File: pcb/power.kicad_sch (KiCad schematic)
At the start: 33 parts, among them U5 REG_LDO_3V3_250mA_TI_LP5907MF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, U7 REG_SW_BOOST_TI_TLV61046ADBV

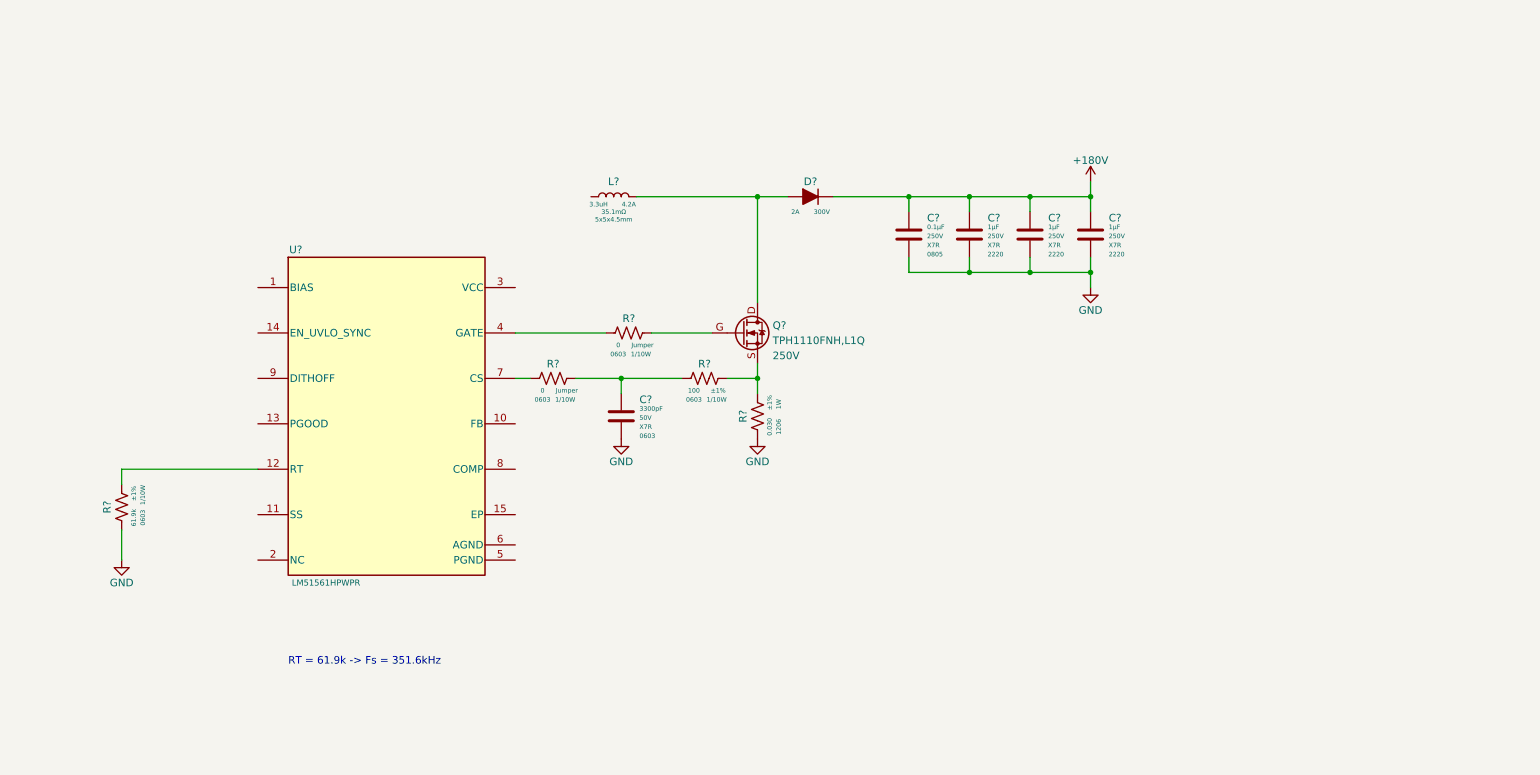
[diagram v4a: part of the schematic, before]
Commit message: Added soft start cap
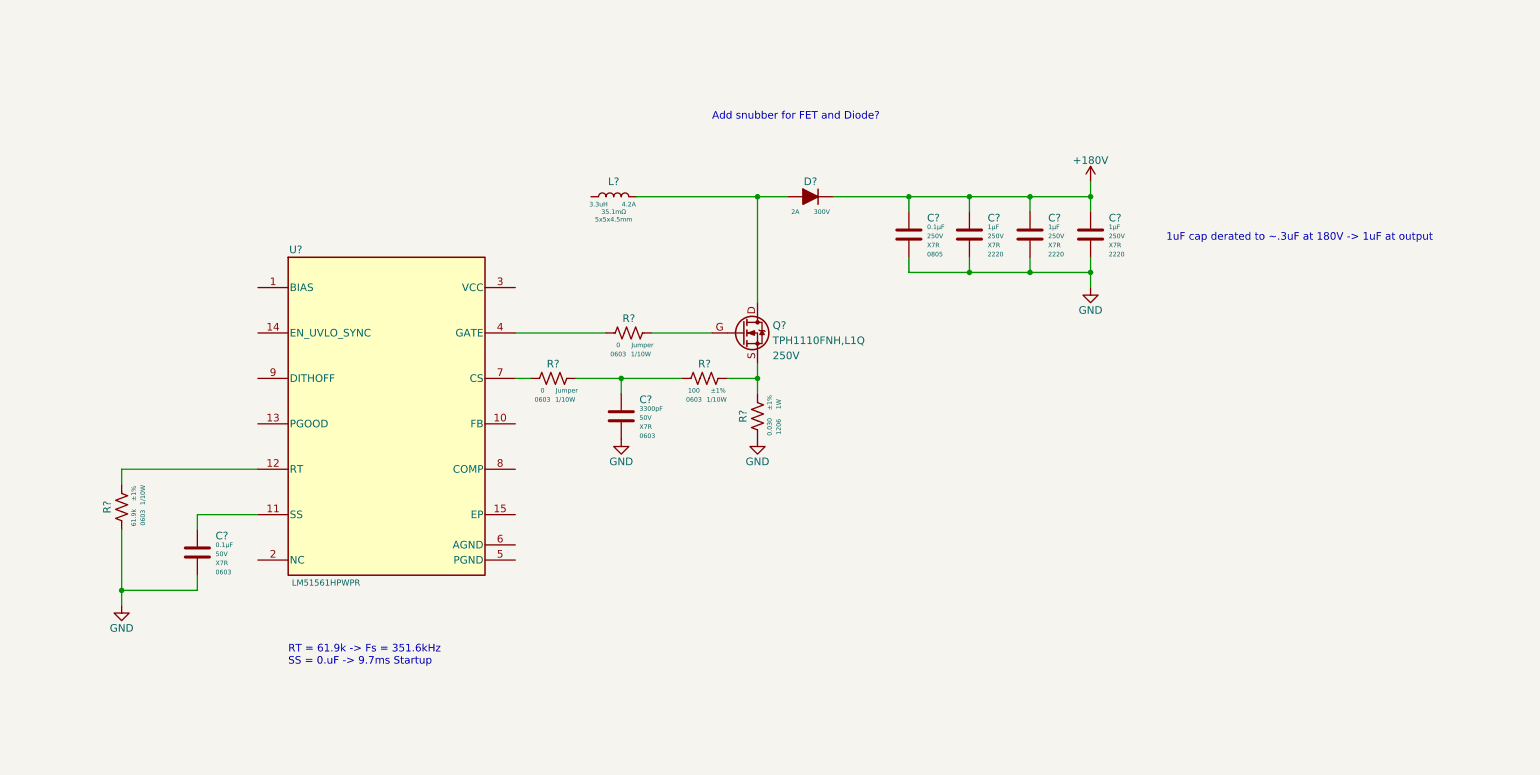
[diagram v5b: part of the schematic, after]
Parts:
- added C?: CAP_CER_0u1_50V_X7R_0603, Capacitor_SMD:C_0603_1608Metric, symbol arjun_symbols:CAP_CER_0u1_50V_X7R_0603
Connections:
- net GND: now also C?.2
- net at U?.11 (SS): now also C?.1
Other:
- note added: "1uF cap derated to ~.3uF at 180V -> 1uF at output"
- note added: "Add snubber for FET and Diode?"
- note added: "RT = 61.9k -> Fs = 351.6kHz SS = 0.uF -> 9.7ms Startup"
- note removed: "RT = 61.9k -> Fs = 351.6kHz"
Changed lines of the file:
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@@
   (junction (at 111.76 215.9) (diameter 0) (color 0 0 0 0)
   )
+  (junction (at 149.86 124.46) (diameter 0) (color 0 0 0 0)
+  )
   (junction (at 139.7 203.2) (diameter 0) (color 0 0 0 0)
   )
@@
     (stroke (width 0) (type default) (color 0 0 0 0))
   )
+  (wire (pts (xy 162.56 124.46) (xy 149.86 124.46))
+    (stroke (width 0) (type default) (color 0 0 0 0))
+  )
   (wire (pts (xy 104.14 73.66) (xy 106.68 73.66))
     (stroke (width 0) (type default) (color 0 0 0 0))
@@
     (stroke (width 0) (type default) (color 0 0 0 0))
   )
+  (wire (pts (xy 162.56 111.76) (xy 172.72 111.76))
+    (stroke (width 0) (type default) (color 0 0 0 0))
+  )
   (wire (pts (xy 88.9 185.42) (xy 99.06 185.42))
     (stroke (width 0) (type default) (color 0 0 0 0))
@@
     (stroke (width 0) (type default) (color 0 0 0 0))
   )
+  (wire (pts (xy 162.56 114.3) (xy 162.56 111.76))
+    (stroke (width 0) (type default) (color 0 0 0 0))
+  )
   (wire (pts (xy 246.38 213.36) (xy 246.38 215.9))
     (stroke (width 0) (type default) (color 0 0 0 0))
@@
     (stroke (width 0) (type default) (color 0 0 0 0))
   )
-  (wire (pts (xy 149.86 114.3) (xy 149.86 119.38))
+  (wire (pts (xy 149.86 114.3) (xy 149.86 124.46))
     (stroke (width 0) (type default) (color 0 0 0 0))
   )
@@
     (stroke (width 0) (type default) (color 0 0 0 0))
   )
+  (wire (pts (xy 149.86 124.46) (xy 149.86 127))
+    (stroke (width 0) (type default) (color 0 0 0 0))
+  )
   (wire (pts (xy 129.54 203.2) (xy 129.54 205.74))
     (stroke (width 0) (type default) (color 0 0 0 0))
@@
   )
   (wire (pts (xy 287.02 200.66) (xy 294.64 200.66))
+    (stroke (width 0) (type default) (color 0 0 0 0))
+  )
+  (wire (pts (xy 162.56 121.92) (xy 162.56 124.46))
     (stroke (width 0) (type default) (color 0 0 0 0))
   )
@@
     (effects (font (size 1.27 1.27)) (justify left bottom))
   )
+  (text "Add snubber for FET and Diode?\n" (at 248.92 45.72 0)
+    (effects (font (size 1.27 1.27)) (justify left bottom))
+  )
   (text "!! Add LEDs\n!! Add Test points\n" (at 21.59 25.4 0)
     (effects (font (size 1.27 1.27)) (justify left bottom))
@@
     (effects (font (size 1.27 1.27)) (justify left bottom))
   )
-  (text "RT = 61.9k -> Fs = 351.6kHz\n" (at 177.8 137.16 0)
+  (text "1uF cap derated to ~.3uF at 180V -> 1uF at output\n"
+    (at 325.12 66.04 0)
+    (effects (font (size 1.27 1.27)) (justify left bottom))
+  )
+  (text "RT = 61.9k -> Fs = 351.6kHz\nSS = 0.uF -> 9.7ms Startup"
+    (at 177.8 137.16 0)
     (effects (font (size 1.27 1.27)) (justify left bottom))
   )
@@
     (pin "1")
   )
-  (symbol (lib_id "power:GND") (at 149.86 119.38 0) (unit 1)
-    (in_bom yes) (on_board yes)
-    (property "Reference" "#PWR?" (id 0) (at 149.86 125.73 0)
-      (effects (font (size 1.27 1.27)) hide)
-    )
-    (property "Value" "GND" (id 1) (at 149.86 123.19 0))
-    (property "Footprint" "" (id 2) (at 149.86 119.38 0)
-      (effects (font (size 1.27 1.27)) hide)
-    )
-    (property "Datasheet" "" (id 3) (at 149.86 119.38 0)
+  (symbol (lib_id "power:GND") (at 149.86 127 0) (unit 1)
+    (in_bom yes) (on_board yes)
+    (property "Reference" "#PWR?" (id 0) (at 149.86 133.35 0)
+      (effects (font (size 1.27 1.27)) hide)
+    )
+    (property "Value" "GND" (id 1) (at 149.86 130.81 0))
+    (property "Footprint" "" (id 2) (at 149.86 127 0)
+      (effects (font (size 1.27 1.27)) hide)
+    )
+    (property "Datasheet" "" (id 3) (at 149.86 127 0)
       (effects (font (size 1.27 1.27)) hide)
     )
@@
     (pin "6")
   )
+  (symbol (lib_id "arjun_symbols:CAP_CER_0u1_50V_X7R_0603") (at 162.56 114.3 0) (unit 1)
+    (in_bom yes) (on_board yes)
+    (property "Reference" "C?" (id 0) (at 165.608 115.316 0)
+      (effects (font (size 1.27 1.27)) (justify left))
+    )
+    (property "Value" "CAP_CER_0u1_50V_X7R_0603" (id 1) (at 170.18 109.855 0)
+      (effects (font (size 1.27 1.27)) (justify left) hide)
+    )
+    (property "Footprint" "Capacitor_SMD:C_0603_1608Metric" (id 2) (at 170.18 111.76 0)
+      (effects (font (size 1.27 1.27)) (justify left) hide)
+    )
+    (property "Datasheet" "https://search.murata.co.jp/Ceramy/image/img/A01X/G101/ENG/GRM21BR61H475KE51-01.pdf" (id 3) (at 170.18 121.92 0)
+      (effects (font (size 1.27 1.27)) (justify left) hide)
+    )
+    (property "Manufacturer" "Samsung Electro-Mechanics" (id 4) (at 170.18 116.84 0)
+      (effects (font (size 1.27 1.27)) (justify left) hide)
+    )
+    (property "ManufacturerPN" "CL10B104KB8NNNC" (id 5) (at 170.18 119.38 0)
+      (effects (font (size 1.27 1.27)) (justify left) hide)
+    )
+    (property "Vendor" "Digi-Key" (id 6) (at 170.18 124.46 0)
+      (effects (font (size 1.27 1.27)) (justify left) hide)
+    )
+    (property "VendorPN" "1276-1000-1-ND" (id 7) (at 170.18 127 0)
+      (effects (font (size 1.27 1.27)) (justify left) hide)
+    )
+    (property "Capacitance" "0.1µF" (id 8) (at 165.608 116.84 0)
+      (effects (font (size 0.762 0.762)) (justify left))
+    )
+    (property "Voltage" "50V" (id 9) (at 165.608 118.364 0)
+      (effects (font (size 0.762 0.762)) (justify left))
+    )
+    (property "Package" "0603" (id 10) (at 165.608 121.412 0)
+      (effects (font (size 0.762 0.762)) (justify left))
+    )
+    (property "Temp Co" "X7R" (id 11) (at 165.608 119.888 0)
+      (effects (font (size 0.762 0.762)) (justify left))
+    )
+    (pin "1")
+    (pin "2")
+  )
   (symbol (lib_id ".arjun:FER_120R_2A_0603") (at 231.14 200.66 0) (unit 1)

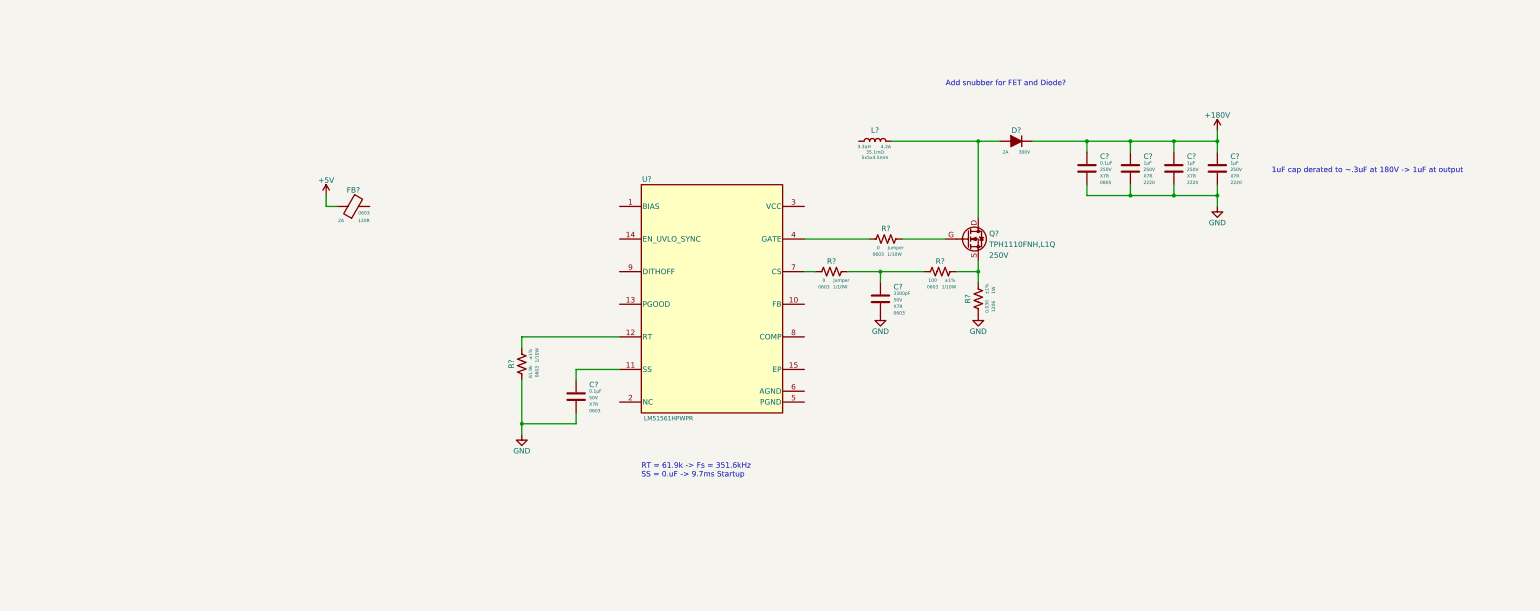
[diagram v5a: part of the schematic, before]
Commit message: Added most of the passives for the 180V supply
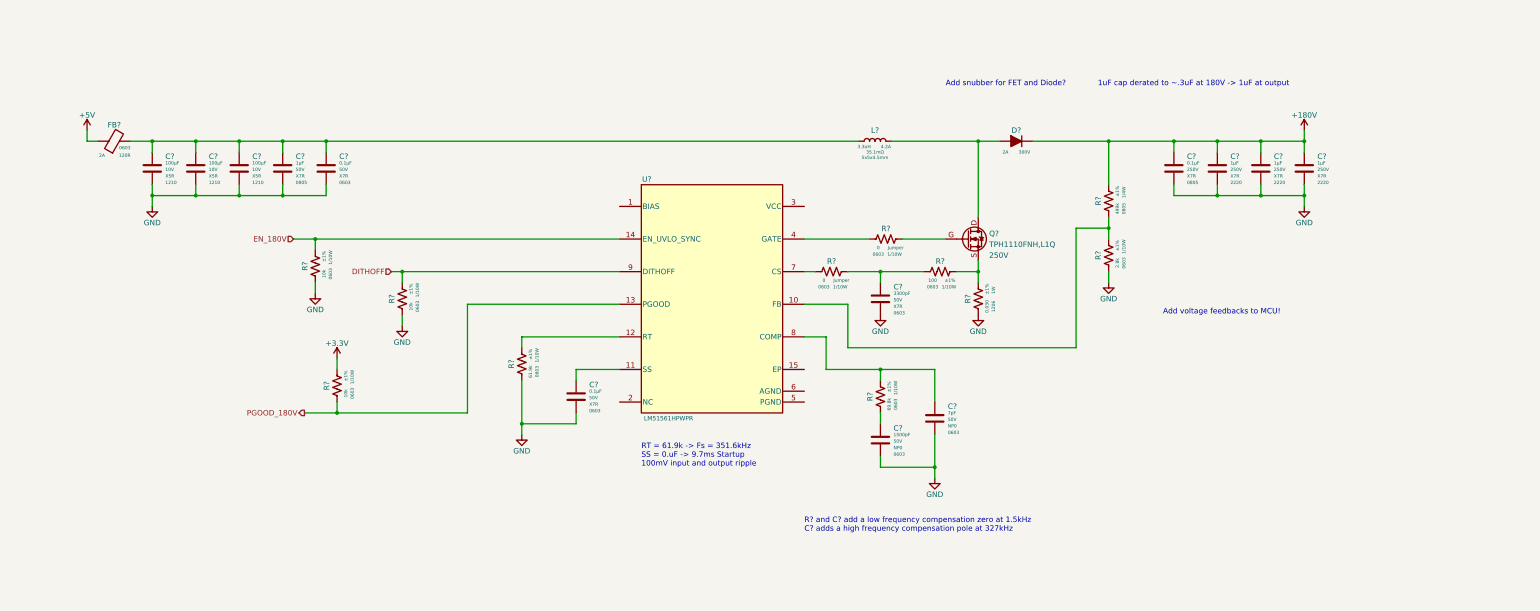
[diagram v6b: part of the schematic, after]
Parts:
- added C? (x3): CAP_CER_100u_10V_X5R_1210, Capacitor_SMD:C_1210_3225Metric, symbol .arjun:CAP_CER_100u_10V_X5R_1210
- added C?: CAP_CER_7p_50V_NP0_0603, Capacitor_SMD:C_0603_1608Metric, symbol .arjun:CAP_CER_7p_50V_NP0_0603
- added C?: CAP_CER_1u_50V_X7R_0805, Capacitor_SMD:C_0805_2012Metric, symbol .arjun:CAP_CER_1u_50V_X7R_0805
- added C?: CAP_CER_1500p_50V_NP0_0603, Capacitor_SMD:C_0603_1608Metric, symbol .arjun:CAP_CER_1500p_50V_NP0_0603
- added C?: CAP_CER_0u1_50V_X7R_0603, Capacitor_SMD:C_0603_1608Metric, symbol arjun_symbols:CAP_CER_0u1_50V_X7R_0603
- added R?: RES_2K8_1P_1/10W_0603, Resistor_SMD:R_0603_1608Metric, symbol .arjun:RES_2K8_1P_1/10W_0603
- added R? (x3): RES_10K_1P_1/10W_0603, Resistor_SMD:R_0603_1608Metric, symbol .arjun:RES_10K_1P_1/10W_0603
- added R?: RES_499K_1P_1/4W_0805, Resistor_SMD:R_0805_2012Metric, symbol .arjun:RES_499K_1P_1/4W_0805
- added R?: RES_69K8_1P_1/10W_0603, Resistor_SMD:R_0603_1608Metric, symbol .arjun:RES_69K8_1P_1/10W_0603
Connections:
- net +3.3V: now also R?.1
- net 180V: now also R?.1
- net GND: now also C?.2, C?.2, C?.2, C?.2, C?.2, C?.2, C?.2, R?.2, R?.2, R?.2
- net at U?.10 (FB): now also R?.1, R?.2
- net PGOOD_180V: now reaches U?.13 (PGOOD)
- net PGOOD_180V: now also R?.2
- net EN_180V: now reaches U?.14 (EN_UVLO_SYNC)
- net EN_180V: now also R?.1
- net at U?.8 (COMP): now also C?.1, R?.1
- net DITHOFF: now reaches U?.9 (DITHOFF)
- net DITHOFF: now also R?.1
- net at FB?.2: now also L?.1, C?.1, C?.1, C?.1, C?.1, C?.1
- new net: C?.1, R?.2
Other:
- note added: "Add voltage feedbacks to MCU!"
- note added: "R? and C? add a low frequency compensation zero at 1.5kHz C? adds a high frequency compensation pole at 327kHz"
- note added: "RT = 61.9k -> Fs = 351.6kHz SS = 0.uF -> 9.7ms Startup 100mV input and output ripple"
- note removed: "RT = 61.9k -> Fs = 351.6kHz SS = 0.uF -> 9.7ms Startup"
- moved on the sheet: C?, FB?

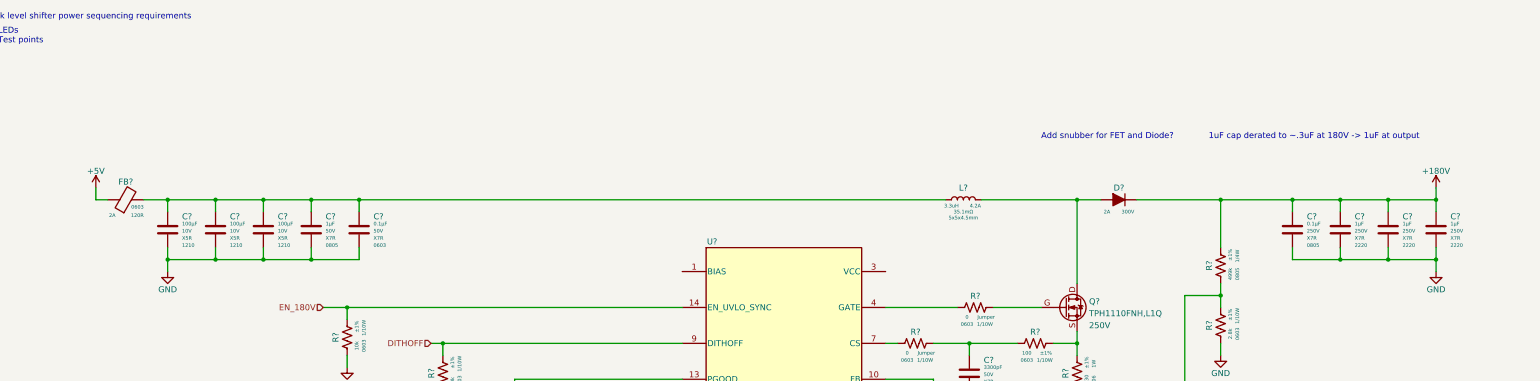
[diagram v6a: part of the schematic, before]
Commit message: Added bypass caps for Bias and Vcc connection to 12V
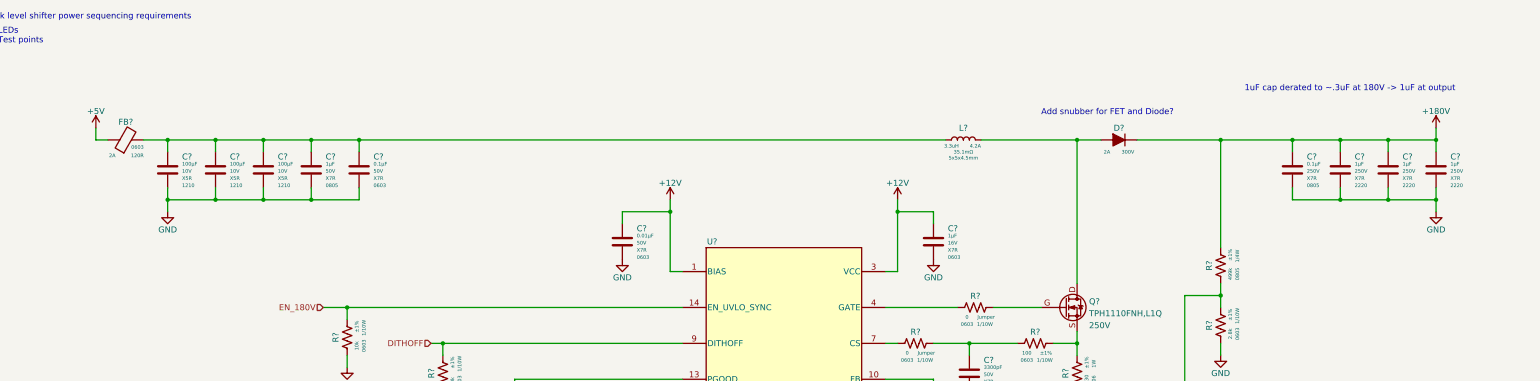
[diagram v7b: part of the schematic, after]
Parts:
- added C?: CAP_CER_0u01_50V_X7R_0603, Capacitor_SMD:C_0603_1608Metric, symbol .arjun:CAP_CER_0u01_50V_X7R_0603
- added C?: CAP_CER_1u_16V_X7R_0603, Capacitor_SMD:C_0603_1608Metric, symbol .arjun:CAP_CER_1u_16V_X7R_0603
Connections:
- net +12V: now also U?.1 (BIAS), U?.3 (VCC), C?.1, C?.1
- net GND: now also C?.2, C?.2
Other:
- moved on the sheet: C?, D?, FB?, L?
